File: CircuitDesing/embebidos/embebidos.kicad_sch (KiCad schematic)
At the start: 17 parts, among them Q1 BSS138

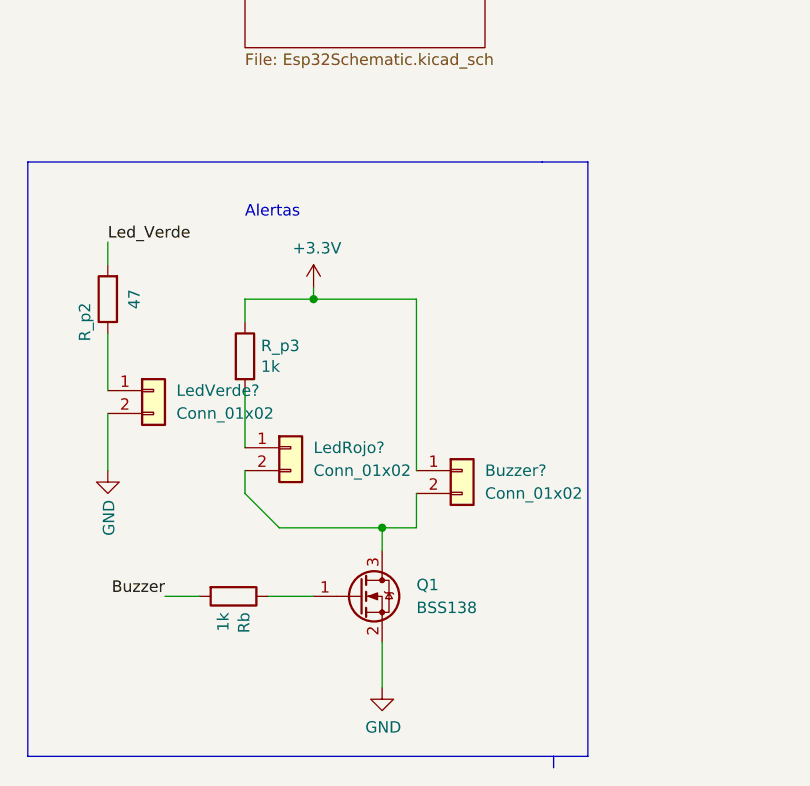
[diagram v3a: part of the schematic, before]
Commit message: Cambio 3.3V en alertas
Cambio 3.3V en alertas
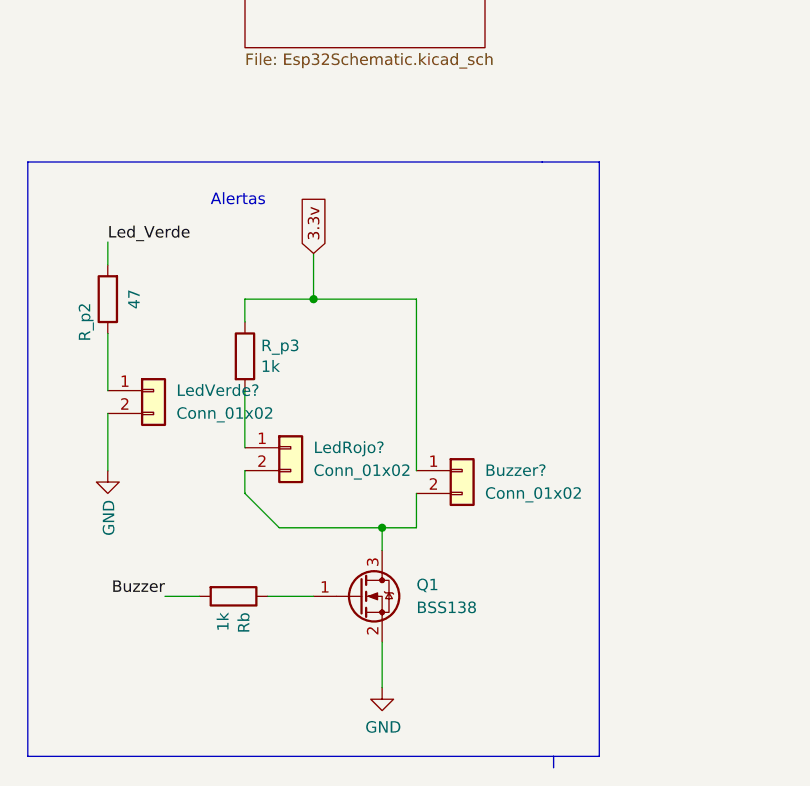
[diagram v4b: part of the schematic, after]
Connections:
- net +3V3 is gone; now on net 3.3v: Buzzer?.1 (Pin_1), R_p3.1
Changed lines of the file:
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@@
-    (stroke (width 0) (type default) (color 0 0 0 0))
-  )
-  (polyline (pts (xy 143.51 114.3) (xy 143.51 180.34))
     (stroke (width 0) (type default) (color 0 0 0 0))
   )
@@
     (stroke (width 0) (type default) (color 0 0 0 0))
   )
-  (wire (pts (xy 113.03 128.27) (xy 113.03 129.54))
+  (wire (pts (xy 113.03 124.46) (xy 113.03 129.54))
     (stroke (width 0) (type default) (color 0 0 0 0))
   )
@@
     (stroke (width 0) (type default) (color 0 0 0 0))
   )
-  (polyline (pts (xy 138.43 114.3) (xy 143.51 114.3))
+  (polyline (pts (xy 138.43 114.3) (xy 144.78 114.3))
     (stroke (width 0) (type default) (color 0 0 0 0))
   )
@@
     (stroke (width 0) (type default) (color 0 0 0 0))
   )
-  (polyline (pts (xy 139.7 180.34) (xy 143.51 180.34))
+  (polyline (pts (xy 139.7 180.34) (xy 144.78 180.34))
+    (stroke (width 0) (type default) (color 0 0 0 0))
+  )
+  (polyline (pts (xy 144.78 114.3) (xy 144.78 180.34))
     (stroke (width 0) (type default) (color 0 0 0 0))
   )
@@
     (stroke (width 0) (type default) (color 0 0 0 0))
   )
-  (text "Alertas" (at 105.41 120.65 0)
+  (text "Alertas" (at 101.6 119.38 0)
     (effects (font (size 1.27 1.27)) (justify left bottom))
   )
@@
     )
   )
+  (global_label "3.3v" (shape input) (at 113.03 124.46 90) (fields_autoplaced)
+    (effects (font (size 1.27 1.27)) (justify left))
+    (property "Intersheet References" "${INTERSHEET_REFS}" (id 0) (at 112.9506 118.0555 90)
+      (effects (font (size 1.27 1.27)) (justify left) hide)
+    )
+  )
   (global_label "3.3v" (shape input) (at 31.75 149.86 180) (fields_autoplaced)
     (effects (font (size 1.27 1.27)) (justify right))
@@
     (pin "1")
     (pin "2")
-  )
-  (symbol (lib_id "DiseñoApp-rescue:+3.3V-power") (at 113.03 128.27 0) (unit 1)
-    (in_bom yes) (on_board yes)
-    (property "Reference" "#PWR?" (id 0) (at 113.03 132.08 0)
-      (effects (font (size 1.27 1.27)) hide)
-    )
-    (property "Value" "+3.3V" (id 1) (at 113.411 123.8758 0))
-    (property "Footprint" "" (id 2) (at 113.03 128.27 0)
-      (effects (font (size 1.27 1.27)) hide)
-    )
-    (property "Datasheet" "" (id 3) (at 113.03 128.27 0)
-      (effects (font (size 1.27 1.27)) hide)
-    )
-    (pin "1")
   )
   (symbol (lib_id "Device:R") (at 31.75 44.45 180) (unit 1)
@@
       (reference "#PWR0109") (unit 1) (value "GND") (footprint "")
     )
-    (path "/22648eea-9362-47c1-852b-9982044237cc"
-      (reference "#PWR?") (unit 1) (value "+3.3V") (footprint "")
-    )
     (path "/baefe8d2-116f-4132-b22d-e866645ad738/4b7297e2-8cf6-43bf-8c84-d013fe580a85"
       (reference "#PWR?") (unit 1) (value "GND") (footprint "")
@@
       (reference "Q4") (unit 1) (value "IRF540N") (footprint "Package_TO_SOT_THT:TO-220-3_Vertical")
     )
+    (path "/baefe8d2-116f-4132-b22d-e866645ad738/98ba4dab-b14f-4738-95bb-dc1c0da7c6a2/cf38a8e6-6607-4565-83b3-309a1bdaae64"
+      (reference "Q?") (unit 1) (value "BSS138") (footprint "Package_TO_SOT_SMD:SOT-23")
+    )
+    (path "/baefe8d2-116f-4132-b22d-e866645ad738/329a0438-132e-4ea6-ad41-5f627ea80d35/cf38a8e6-6607-4565-83b3-309a1bdaae64"
+      (reference "Q?") (unit 1) (value "BSS138") (footprint "Package_TO_SOT_SMD:SOT-23")
+    )
     (path "/baefe8d2-116f-4132-b22d-e866645ad738/6883cda8-9c83-4f43-b6c5-936142ee57ec/cf38a8e6-6607-4565-83b3-309a1bdaae64"
       (reference "Q?") (unit 1) (value "BSS138") (footprint "Package_TO_SOT_SMD:SOT-23")
     )
-    (path "/baefe8d2-116f-4132-b22d-e866645ad738/98ba4dab-b14f-4738-95bb-dc1c0da7c6a2/cf38a8e6-6607-4565-83b3-309a1bdaae64"
-      (reference "Q?") (unit 1) (value "BSS138") (footprint "Package_TO_SOT_SMD:SOT-23")
-    )
-    (path "/baefe8d2-116f-4132-b22d-e866645ad738/329a0438-132e-4ea6-ad41-5f627ea80d35/cf38a8e6-6607-4565-83b3-309a1bdaae64"
-      (reference "Q?") (unit 1) (value "BSS138") (footprint "Package_TO_SOT_SMD:SOT-23")
-    )
     (path "/4a4a8db1-1786-4804-b37e-204adf7255cc/3bbf86fb-9c3d-4041-add8-b662fd19d6ee/cf38a8e6-6607-4565-83b3-309a1bdaae64"
       (reference "Q?") (unit 1) (value "BSS138") (footprint "Package_TO_SOT_SMD:SOT-23")
     )
+    (path "/baefe8d2-116f-4132-b22d-e866645ad738/329a0438-132e-4ea6-ad41-5f627ea80d35/d5d169e6-b703-4deb-bae6-ffa604c65d36"
+      (reference "Q?") (unit 1) (value "BSS138") (footprint "Package_TO_SOT_SMD:SOT-23")
+    )
     (path "/baefe8d2-116f-4132-b22d-e866645ad738/564765a6-2a30-47eb-84d6-741ce30487fa/d5d169e6-b703-4deb-bae6-ffa604c65d36"
       (reference "Q?") (unit 1) (value "BSS138") (footprint "Package_TO_SOT_SMD:SOT-23")
     )
-    (path "/baefe8d2-116f-4132-b22d-e866645ad738/329a0438-132e-4ea6-ad41-5f627ea80d35/d5d169e6-b703-4deb-bae6-ffa604c65d36"
+    (path "/4a4a8db1-1786-4804-b37e-204adf7255cc/3bbf86fb-9c3d-4041-add8-b662fd19d6ee/d5d169e6-b703-4deb-bae6-ffa604c65d36"
+      (reference "Q?") (unit 1) (value "BSS138") (footprint "Package_TO_SOT_SMD:SOT-23")
+    )
+    (path "/baefe8d2-116f-4132-b22d-e866645ad738/6883cda8-9c83-4f43-b6c5-936142ee57ec/d5d169e6-b703-4deb-bae6-ffa604c65d36"
       (reference "Q?") (unit 1) (value "BSS138") (footprint "Package_TO_SOT_SMD:SOT-23")
     )
@@
       (reference "Q?") (unit 1) (value "BSS138") (footprint "Package_TO_SOT_SMD:SOT-23")
     )
-    (path "/4a4a8db1-1786-4804-b37e-204adf7255cc/3bbf86fb-9c3d-4041-add8-b662fd19d6ee/d5d169e6-b703-4deb-bae6-ffa604c65d36"
-      (reference "Q?") (unit 1) (value "BSS138") (footprint "Package_TO_SOT_SMD:SOT-23")
-    )
-    (path "/baefe8d2-116f-4132-b22d-e866645ad738/6883cda8-9c83-4f43-b6c5-936142ee57ec/d5d169e6-b703-4deb-bae6-ffa604c65d36"
-      (reference "Q?") (unit 1) (value "BSS138") (footprint "Package_TO_SOT_SMD:SOT-23")
-    )
     (path "/255ea3b8-af73-4dd8-9773-761204920633/1fced78e-da3b-4a07-b26f-1446114df708"
       (reference "R1") (unit 1) (value "10k") (footprint "Resistor_SMD:R_0603_1608Metric_Pad0.98x0.95mm_HandSolder")
@@
       (reference "R2") (unit 1) (value "1k") (footprint "Resistor_SMD:R_0603_1608Metric_Pad0.98x0.95mm_HandSolder")
     )
+    (path "/baefe8d2-116f-4132-b22d-e866645ad738/564765a6-2a30-47eb-84d6-741ce30487fa/3fb99e89-8ea9-487a-b85f-a149b05529c5"
+      (reference "R2") (unit 1) (value "10k") (footprint "Resistor_SMD:R_0603_1608Metric_Pad0.98x0.95mm_HandSolder")
+    )
     (path "/4a4a8db1-1786-4804-b37e-204adf7255cc/3bbf86fb-9c3d-4041-add8-b662fd19d6ee/3fb99e89-8ea9-487a-b85f-a149b05529c5"
       (reference "R2") (unit 1) (value "10k") (footprint "Resistor_SMD:R_0603_1608Metric_Pad0.98x0.95mm_HandSolder")
     )
-    (path "/baefe8d2-116f-4132-b22d-e866645ad738/564765a6-2a30-47eb-84d6-741ce30487fa/3fb99e89-8ea9-487a-b85f-a149b05529c5"
-      (reference "R2") (unit 1) (value "10k") (footprint "Resistor_SMD:R_0603_1608Metric_Pad0.98x0.95mm_HandSolder")
-    )
     (path "/baefe8d2-116f-4132-b22d-e866645ad738/09e4f7c4-4e47-4ddf-861c-78dab24f1b9c"
       (reference "R3") (unit 1) (value "1k") (footprint "Resistor_SMD:R_0603_1608Metric_Pad0.98x0.95mm_HandSolder")
@@
       (reference "R9") (unit 1) (value "1k") (footprint "Resistor_SMD:R_0603_1608Metric_Pad0.98x0.95mm_HandSolder")
     )
+    (path "/baefe8d2-116f-4132-b22d-e866645ad738/329a0438-132e-4ea6-ad41-5f627ea80d35/576d0313-f868-436d-bd38-883c81dc3444"
+      (reference "R?") (unit 1) (value "10k") (footprint "Resistor_SMD:R_0603_1608Metric_Pad0.98x0.95mm_HandSolder")
+    )
     (path "/baefe8d2-116f-4132-b22d-e866645ad738/564765a6-2a30-47eb-84d6-741ce30487fa/576d0313-f868-436d-bd38-883c81dc3444"
       (reference "R?") (unit 1) (value "10k") (footprint "Resistor_SMD:R_0603_1608Metric_Pad0.98x0.95mm_HandSolder")
     )
-    (path "/baefe8d2-116f-4132-b22d-e866645ad738/329a0438-132e-4ea6-ad41-5f627ea80d35/576d0313-f868-436d-bd38-883c81dc3444"
+    (path "/baefe8d2-116f-4132-b22d-e866645ad738/98ba4dab-b14f-4738-95bb-dc1c0da7c6a2/576d0313-f868-436d-bd38-883c81dc3444"
       (reference "R?") (unit 1) (value "10k") (footprint "Resistor_SMD:R_0603_1608Metric_Pad0.98x0.95mm_HandSolder")
     )
@@
       (reference "R?") (unit 1) (value "10k") (footprint "Resistor_SMD:R_0603_1608Metric_Pad0.98x0.95mm_HandSolder")
     )
-    (path "/baefe8d2-116f-4132-b22d-e866645ad738/98ba4dab-b14f-4738-95bb-dc1c0da7c6a2/576d0313-f868-436d-bd38-883c81dc3444"
+    (path "/baefe8d2-116f-4132-b22d-e866645ad738/329a0438-132e-4ea6-ad41-5f627ea80d35/6d147a77-64d1-441f-8a6a-fd37182f0499"
+      (reference "R?") (unit 1) (value "10k") (footprint "Resistor_SMD:R_0603_1608Metric_Pad0.98x0.95mm_HandSolder")
+    )
+    (path "/baefe8d2-116f-4132-b22d-e866645ad738/6883cda8-9c83-4f43-b6c5-936142ee57ec/6d147a77-64d1-441f-8a6a-fd37182f0499"
+      (reference "R?") (unit 1) (value "10k") (footprint "Resistor_SMD:R_0603_1608Metric_Pad0.98x0.95mm_HandSolder")
+    )
+    (path "/baefe8d2-116f-4132-b22d-e866645ad738/98ba4dab-b14f-4738-95bb-dc1c0da7c6a2/6d147a77-64d1-441f-8a6a-fd37182f0499"
       (reference "R?") (unit 1) (value "10k") (footprint "Resistor_SMD:R_0603_1608Metric_Pad0.98x0.95mm_HandSolder")
     )
@@
       (reference "R?") (unit 1) (value "10k") (footprint "Resistor_SMD:R_0603_1608Metric_Pad0.98x0.95mm_HandSolder")
     )
-    (path "/baefe8d2-116f-4132-b22d-e866645ad738/329a0438-132e-4ea6-ad41-5f627ea80d35/6d147a77-64d1-441f-8a6a-fd37182f0499"
-      (reference "R?") (unit 1) (value "10k") (footprint "Resistor_SMD:R_0603_1608Metric_Pad0.98x0.95mm_HandSolder")
-    )
-    (path "/baefe8d2-116f-4132-b22d-e866645ad738/98ba4dab-b14f-4738-95bb-dc1c0da7c6a2/6d147a77-64d1-441f-8a6a-fd37182f0499"
-      (reference "R?") (unit 1) (value "10k") (footprint "Resistor_SMD:R_0603_1608Metric_Pad0.98x0.95mm_HandSolder")
-    )
-    (path "/baefe8d2-116f-4132-b22d-e866645ad738/6883cda8-9c83-4f43-b6c5-936142ee57ec/6d147a77-64d1-441f-8a6a-fd37182f0499"
-      (reference "R?") (unit 1) (value "10k") (footprint "Resistor_SMD:R_0603_1608Metric_Pad0.98x0.95mm_HandSolder")
-    )

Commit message: Ruteo completo
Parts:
- removed J_prog1: Conn_01x06_Male, Connector_PinHeader_2.54mm:PinHeader_1x06_P2.54mm_Horizontal, symbol Connector:Conn_01x06_Male
- added J1: Conn_01x03_Male, Connector_PinHeader_2.54mm:PinHeader_1x03_P2.54mm_Vertical, symbol Connector:Conn_01x03_Male
- Buzzer1: renamed from Buzzer?; footprint (none) -> Connector_JST:JST_EH_B2B-EH-A_1x02_P2.50mm_Vertical
- LedRojo1: renamed from LedRojo?; footprint (none) -> Connector_JST:JST_EH_B2B-EH-A_1x02_P2.50mm_Vertical
- LedVerde1: renamed from LedVerde?; footprint (none) -> Connector_JST:JST_EH_B2B-EH-A_1x02_P2.50mm_Vertical
- R_p3: footprint (none) -> Resistor_SMD:R_0805_2012Metric_Pad1.20x1.40mm_HandSolder
- renumbered Botones_M to Botones_M1, Pantalla-I2C to Pantalla-I2C1, RCL2 to RCL1, RCL1 to RCL2, RDA2 to RDA1, RDA1 to RDA2, Rb to Rb1
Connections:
- net 3.3v: now also Buzzer1.2 (Pin_2); no longer Buzzer1.1 (Pin_1)
- net GND: now also J1.3 (Pin_3)
- net Prog_Rx: now also J1.1 (Pin_1)
- net Prog_Tx: now also J1.2 (Pin_2)
- net at LedRojo1.2 (Pin_2), Q1.3 (D): now also Buzzer1.1 (Pin_1); no longer Buzzer1.2 (Pin_2)
- no-connect marks 3 -> 0
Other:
- sheet Potencia ports: added 5V; removed out_5v
- moved on the sheet: Buzzer1
